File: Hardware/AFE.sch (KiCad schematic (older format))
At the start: 43 parts, among them U801 4069.HEF4069UBTT,118, U802 MCP47CXBX2

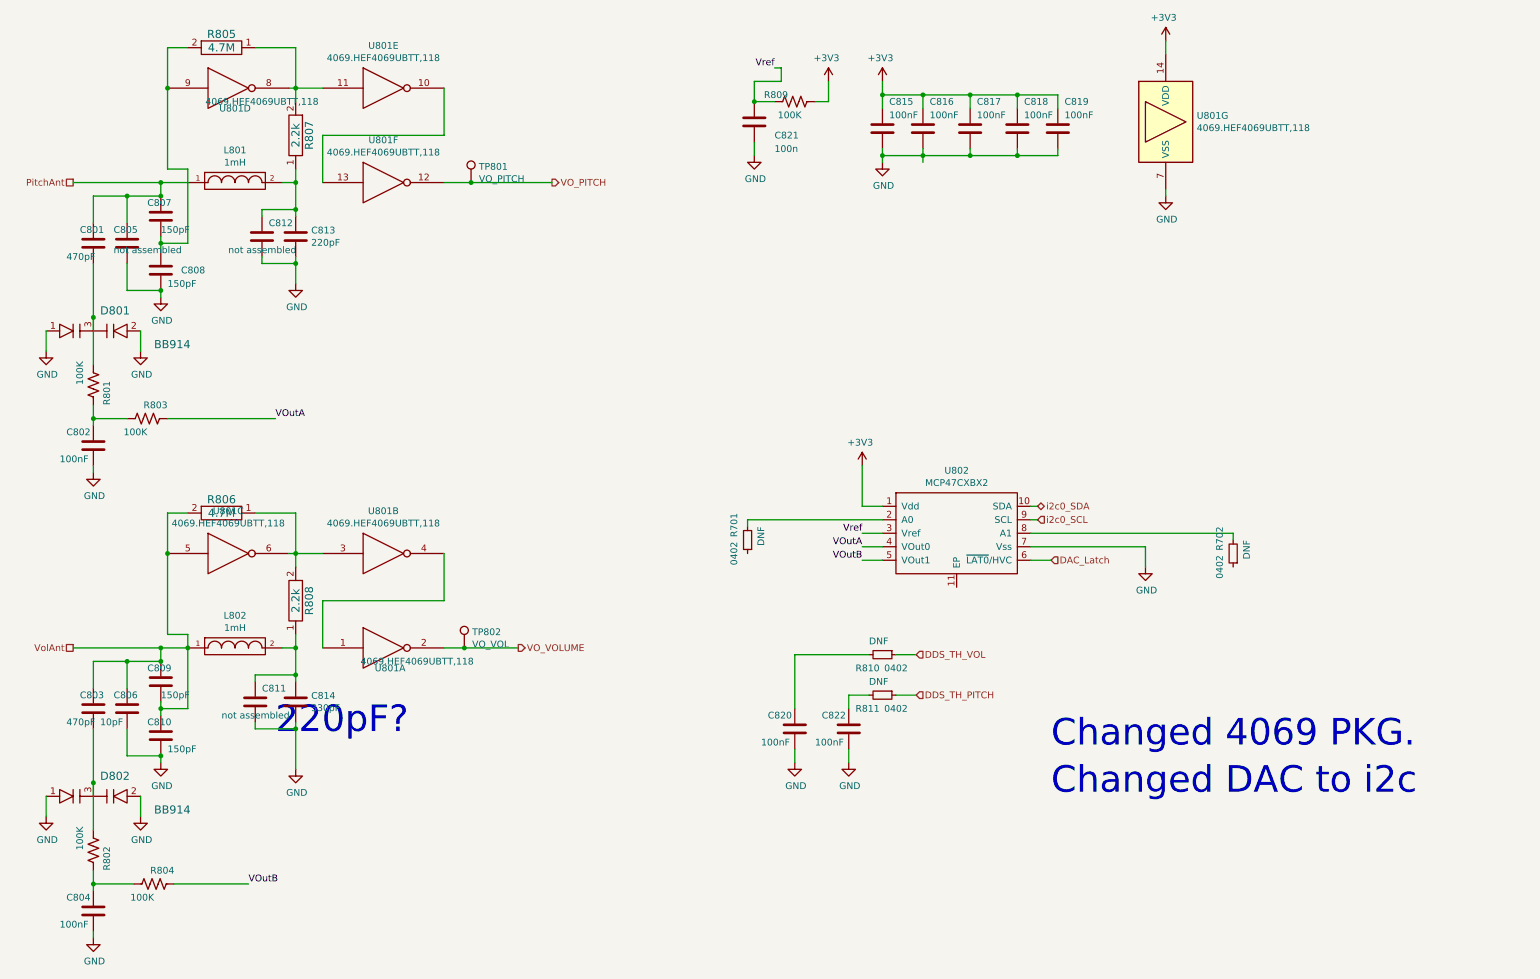
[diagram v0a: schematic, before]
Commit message: Fixing up some BoM repetition.
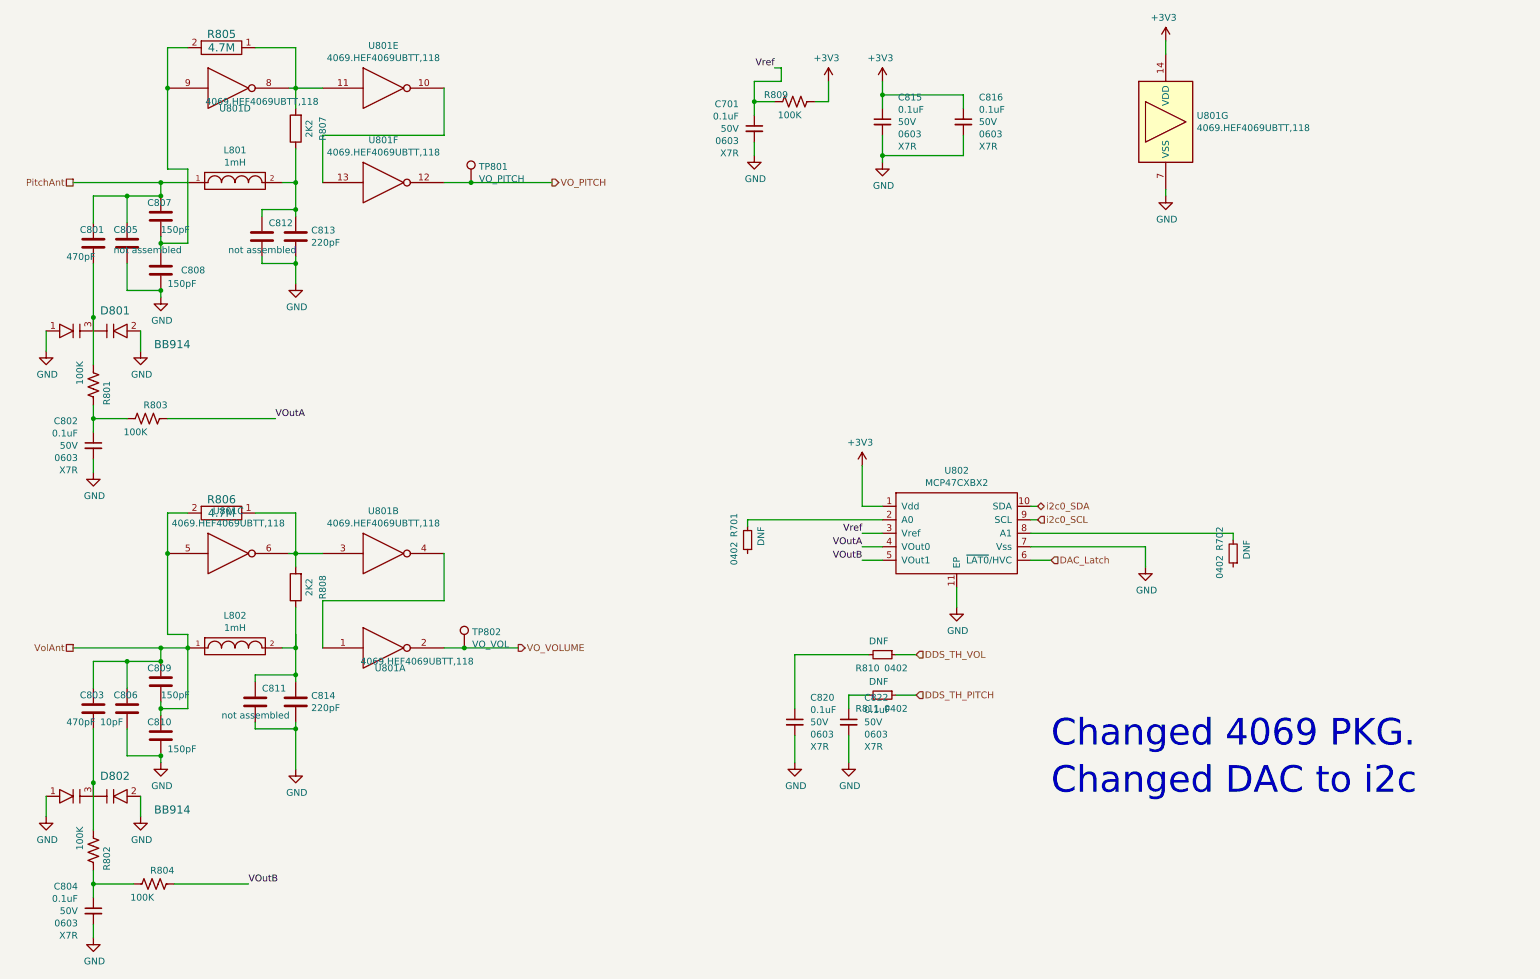
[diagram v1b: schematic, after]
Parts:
- removed C802, C804, C815, C816, C817, C818, C819, C820, C822: 100nF, Capacitor_SMD:C_0603_1608Metric_Pad1.08x0.95mm_HandSolder, symbol Device:C
- removed C821: 100n, Capacitor_SMD:C_0603_1608Metric_Pad1.08x0.95mm_HandSolder, symbol Device:C
- removed R807, R808: 2.2k, Resistor_SMD:R_0603_1608Metric_Pad0.98x0.95mm_HandSolder, symbol OpenThereminCC-rescue:RES
- added C701, C802, C804, C815, C816, C820, C822: 0.1uF, Capacitor_SMD:C_0603_1608Metric, symbol Device:C_Small
- added R807, R808: 2K2, Resistor_SMD:R_0603_1608Metric, symbol Device:R
- C813: footprint Capacitor_SMD:C_0603_1608Metric_Pad1.08x0.95mm_HandSolder -> Capacitor_SMD:C_0603_1608Metric
- C814: value 330pF -> 220pF
- R805, R806: footprint Resistor_SMD:R_0603_1608Metric_Pad0.98x0.95mm_HandSolder -> Resistor_SMD:R_0603_1608Metric
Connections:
- net +3V3: now also C815.1, C816.1
- net GND: now also U802.11 (EP), C701.2, C802.2, C804.2, C815.2, C816.2, C820.2, C822.2
- net Vref: now also C701.1
- net at R806.1, U801.3, U801.6: now also R808.2
- net at C812.1, C813.1, L801.2: now also R807.1
- net at R805.1, U801.11, U801.8: now also R807.2
- net at R801.2, R803.1: now also C802.1
- net at C811.1, C814.1, L802.2: now also R808.1
- net at R802.2, R804.1: now also C804.1
- net at R811.2: now also C822.1
- net at R810.2: now also C820.1
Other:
- note removed: "220pF?\n"

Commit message: Placements mostly done.
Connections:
- net at C804.1, R802.2: no longer R804.1
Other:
- moved on the sheet: R804
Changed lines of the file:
@@
 L Device:R_US R?
 U 1 1 6165DF0B
-P 1500 7000
+P 1550 7000
 AR Path="/611E335F/6165DF0B" Ref="R?"  Part="1"
 AR Path="/612429E8/6165DF0B" Ref="R804"  Part="1"
-F 0 "R804" V 1600 6850 50  0000 L CNN
-F 1 "100K" V 1400 7000 50  0000 L CNN
-F 2 "Resistor_SMD:R_0603_1608Metric" V 1430 7000 50  0001 C CNN
-F 3 "~" H 1500 7000 50  0001 C CNN
-F 4 "0603" H 1500 7000 50  0001 C CNN "Pkg"
-F 5 "ESR03EZPJ104" H 1500 7000 50  0001 C CNN "MPN"
-F 6 "RHM100KDCT-ND" H 1500 7000 50  0001 C CNN "DPN"
-	1    1500 7000
+F 0 "R804" V 1650 6850 50  0000 L CNN
+F 1 "100K" V 1450 7000 50  0000 L CNN
+F 2 "Resistor_SMD:R_0603_1608Metric" V 1480 7000 50  0001 C CNN
+F 3 "~" H 1550 7000 50  0001 C CNN
+F 4 "0603" H 1550 7000 50  0001 C CNN "Pkg"
+F 5 "ESR03EZPJ104" H 1550 7000 50  0001 C CNN "MPN"
+F 6 "RHM100KDCT-ND" H 1550 7000 50  0001 C CNN "DPN"
+	1    1550 7000
 	0    -1   -1   0
 $EndComp
 Wire Wire Line
-	1650 7000 2200 7000
+	1700 7000 2250 7000
 Wire Wire Line
 	1050 7000 1350 7000

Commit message: Most placements, testpoints and spare points added. Looking good.
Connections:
- net VO_PITCH: now also C822.1, R811.2
- net VO_VOLUME: now also C820.1, R810.2
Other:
- note removed: "Changed 4069 PKG."
- note removed: "Changed DAC to i2c"
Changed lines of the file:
@@
 Wire Wire Line
 	2550 2400 2550 2550
-Text Notes 8150 6350 0    197  ~ 0
-Changed DAC to i2c
 $Comp
 L OHMC2022:MCP47CXBX2 U802
@@
 Text HLabel 900  5250 0    50   UnSpc ~ 0
 VolAnt
-Text HLabel 4450 1800 2    50   Output ~ 0
+Text HLabel 4950 1800 2    50   Output ~ 0
 VO_PITCH
-Text HLabel 4200 5250 2    50   Output ~ 0
+Text HLabel 4700 5250 2    50   Output ~ 0
 VO_VOLUME
 Text HLabel 8050 4200 2    50   BiDi ~ 0
@@
 Wire Wire Line
 	1750 5250 1750 5150
-Text Notes 8150 6000 0    197  ~ 0
-Changed 4069 PKG.
 Wire Wire Line
 	900  1800 1550 1800
@@
 Connection ~ 3800 5250
 Wire Wire Line
-	3800 5250 4200 5250
+	3800 5250 4700 5250
 Wire Wire Line
 	3650 1800 3850 1800
 Connection ~ 3850 1800
 Wire Wire Line
-	3850 1800 4450 1800
+	3850 1800 4950 1800
 Wire Wire Line
 	6750 4500 6900 4500
@@
 Wire Wire Line
 	2550 4950 2550 5250
+Text Label 4200 5250 0    50   ~ 0
+VO_VOLUME
+Text Label 6250 5300 0    50   ~ 0
+VO_VOLUME
+Text Label 4450 1800 0    50   ~ 0
+VO_PITCH
+Text Label 6700 5600 2    50   ~ 0
+VO_PITCH
 $EndSCHEMATC

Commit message: Spare points on r=26.5mm @ x1.27mm linear separation.
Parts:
- added JP?: DAC_A0, OHMC2022:SolderJumper-3_P1.3mm_Open_RoundedPad1.0x1.5mm, symbol Jumper:SolderJumper_3_Open
- added JP?: DAC_A1, OHMC2022:SolderJumper-3_P1.3mm_Open_RoundedPad1.0x1.5mm, symbol Jumper:SolderJumper_3_Open
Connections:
- wire segments 138 -> 141
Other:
- moved on the sheet: R701, R702
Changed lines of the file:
@@
 L Device:R_Small R?
 U 1 1 614FE799
-P 5900 4450
+P 6400 4300
 AR Path="/611E335F/614FE799" Ref="R?"  Part="1"
 AR Path="/614FE799" Ref="R?"  Part="1"
 AR Path="/611E3335/614FE799" Ref="R?"  Part="1"
 AR Path="/612429E8/614FE799" Ref="R701"  Part="1"
-F 0 "R701" V 6000 4250 50  0000 L CNN
-F 1 "DNF" V 5800 4350 50  0000 L CNN
-F 2 "Resistor_SMD:R_0402_1005Metric" V 5830 4450 50  0001 C CNN
-F 3 "~" H 5900 4450 50  0001 C CNN
-F 4 "0402" V 6000 4550 50  0000 C CNN "Pkg"
-F 5 "" H 5900 4450 50  0001 C CNN "MPN"
-F 6 "" H 5900 4450 50  0001 C CNN "DPN"
-	1    5900 4450
-	-1   0    0    1
+F 0 "R701" V 6500 4100 50  0000 L CNN
+F 1 "DNF" V 6300 4200 50  0000 L CNN
+F 2 "Resistor_SMD:R_0402_1005Metric" V 6330 4300 50  0001 C CNN
+F 3 "~" H 6400 4300 50  0001 C CNN
+F 4 "0402" V 6500 4400 50  0000 C CNN "Pkg"
+F 5 "" H 6400 4300 50  0001 C CNN "MPN"
+F 6 "" H 6400 4300 50  0001 C CNN "DPN"
+	1    6400 4300
+	0    -1   -1   0
 $EndComp
 $Comp
 L Device:R_Small R?
 U 1 1 614FEE62
-P 9500 4550
+P 9000 4400
 AR Path="/611E335F/614FEE62" Ref="R?"  Part="1"
 AR Path="/614FEE62" Ref="R?"  Part="1"
 AR Path="/611E3335/614FEE62" Ref="R?"  Part="1"
 AR Path="/612429E8/614FEE62" Ref="R702"  Part="1"
-F 0 "R702" V 9600 4350 50  0000 L CNN
-F 1 "DNF" V 9400 4450 50  0000 L CNN
-F 2 "Resistor_SMD:R_0402_1005Metric" V 9430 4550 50  0001 C CNN
-F 3 "~" H 9500 4550 50  0001 C CNN
-F 4 "0402" V 9600 4650 50  0000 C CNN "Pkg"
-F 5 "" H 9500 4550 50  0001 C CNN "MPN"
-F 6 "" H 9500 4550 50  0001 C CNN "DPN"
-	1    9500 4550
-	-1   0    0    1
-$EndComp
-Wire Wire Line
-	8000 4400 9500 4400
-Wire Wire Line
-	9500 4400 9500 4450
-Wire Wire Line
-	5900 4300 5900 4350
-Wire Wire Line
-	5900 4300 6900 4300
+F 0 "R702" V 9100 4200 50  0000 L CNN
+F 1 "DNF" V 8900 4300 50  0000 L CNN
+F 2 "Resistor_SMD:R_0402_1005Metric" V 8930 4400 50  0001 C CNN
+F 3 "~" H 9000 4400 50  0001 C CNN
+F 4 "0402" V 9100 4500 50  0000 C CNN "Pkg"
+F 5 "" H 9000 4400 50  0001 C CNN "MPN"
+F 6 "" H 9000 4400 50  0001 C CNN "DPN"
+	1    9000 4400
+	0    -1   -1   0
+$EndComp
+Wire Wire Line
+	8000 4400 8900 4400
+Wire Wire Line
+	6500 4300 6900 4300
 $Comp
 L power:GND #PWR0141
@@
 Text Label 6700 5600 2    50   ~ 0
 VO_PITCH
+$Comp
+L Jumper:SolderJumper_3_Open JP?
+U 1 1 61714625
+P 6150 4300
+AR Path="/61714625" Ref="JP?"  Part="1"
+AR Path="/612429E8/61714625" Ref="JP?"  Part="1"
+F 0 "JP?" H 6150 4505 50  0000 C CNN
+F 1 "DAC_A0" H 6150 4414 50  0000 C CNN
+F 2 "OHMC2022:SolderJumper-3_P1.3mm_Open_RoundedPad1.0x1.5mm" H 6150 4300 50  0001 C CNN
+F 3 "~" H 6150 4300 50  0001 C CNN
+	1    6150 4300
+	0    -1   -1   0
+$EndComp
+$Comp
+L Jumper:SolderJumper_3_Open JP?
+U 1 1 61720361
+P 9250 4400
+AR Path="/61720361" Ref="JP?"  Part="1"
+AR Path="/612429E8/61720361" Ref="JP?"  Part="1"
+F 0 "JP?" H 9250 4605 50  0000 C CNN
+F 1 "DAC_A1" H 9250 4514 50  0000 C CNN
+F 2 "OHMC2022:SolderJumper-3_P1.3mm_Open_RoundedPad1.0x1.5mm" H 9250 4400 50  0001 C CNN
+F 3 "~" H 9250 4400 50  0001 C CNN
+	1    9250 4400
+	0    1    -1   0
+$EndComp
+$Comp
+L power:+3V3 #PWR?
+U 1 1 6172140B
+P 6150 3900
+AR Path="/611E3335/6172140B" Ref="#PWR?"  Part="1"
+AR Path="/6172140B" Ref="#PWR?"  Part="1"
+AR Path="/612429E8/6172140B" Ref="#PWR?"  Part="1"
+F 0 "#PWR?" H 6150 3750 50  0001 C CNN
+F 1 "+3V3" H 6165 4073 50  0000 C CNN
+F 2 "" H 6150 3900 50  0001 C CNN
+F 3 "" H 6150 3900 50  0001 C CNN
+	1    6150 3900
+	-1   0    0    -1
+$EndComp
+Wire Wire Line
+	6150 3900 6150 4100
+$Comp
+L power:GND #PWR?
+U 1 1 617275D5
+P 6150 4650
+F 0 "#PWR?" H 6150 4400 50  0001 C CNN
+F 1 "GND" H 6158 4477 50  0000 C CNN
+F 2 "" H 6150 4650 50  0000 C CNN
+F 3 "" H 6150 4650 50  0000 C CNN
+	1    6150 4650
+	1    0    0    -1
+$EndComp
+Wire Wire Line
+	6150 4500 6150 4650
+$Comp
+L power:+3V3 #PWR?
+U 1 1 6172EEF6
+P 9250 4000
+AR Path="/611E3335/6172EEF6" Ref="#PWR?"  Part="1"
+AR Path="/6172EEF6" Ref="#PWR?"  Part="1"
+AR Path="/612429E8/6172EEF6" Ref="#PWR?"  Part="1"
+F 0 "#PWR?" H 9250 3850 50  0001 C CNN
+F 1 "+3V3" H 9265 4173 50  0000 C CNN
+F 2 "" H 9250 4000 50  0001 C CNN
+F 3 "" H 9250 4000 50  0001 C CNN
+	1    9250 4000
+	-1   0    0    -1
+$EndComp
+Wire Wire Line
+	9250 4000 9250 4200
+$Comp
+L power:GND #PWR?
+U 1 1 6173729C
+P 9250 4700
+F 0 "#PWR?" H 9250 4450 50  0001 C CNN
+F 1 "GND" H 9258 4527 50  0000 C CNN
+F 2 "" H 9250 4700 50  0000 C CNN
+F 3 "" H 9250 4700 50  0000 C CNN
+	1    9250 4700
+	1    0    0    -1
+$EndComp
+Wire Wire Line
+	9250 4550 9250 4600
+Connection ~ 9250 4600
+Wire Wire Line
+	9250 4600 9250 4700
 $EndSCHEMATC

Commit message: Doing finer aspirational placements.
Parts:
- gave numbers to parts that had none: 2
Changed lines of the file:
@@
 P 6150 4300
 AR Path="/61714625" Ref="JP?"  Part="1"
-AR Path="/612429E8/61714625" Ref="JP?"  Part="1"
-F 0 "JP?" H 6150 4505 50  0000 C CNN
+AR Path="/612429E8/61714625" Ref="JP401"  Part="1"
+F 0 "JP401" H 6150 4505 50  0000 C CNN
 F 1 "DAC_A0" H 6150 4414 50  0000 C CNN
 F 2 "OHMC2022:SolderJumper-3_P1.3mm_Open_RoundedPad1.0x1.5mm" H 6150 4300 50  0001 C CNN
@@
 P 9250 4400
 AR Path="/61720361" Ref="JP?"  Part="1"
-AR Path="/612429E8/61720361" Ref="JP?"  Part="1"
-F 0 "JP?" H 9250 4605 50  0000 C CNN
+AR Path="/612429E8/61720361" Ref="JP402"  Part="1"
+F 0 "JP402" H 9250 4605 50  0000 C CNN
 F 1 "DAC_A1" H 9250 4514 50  0000 C CNN
 F 2 "OHMC2022:SolderJumper-3_P1.3mm_Open_RoundedPad1.0x1.5mm" H 9250 4400 50  0001 C CNN
@@
 AR Path="/611E3335/6172140B" Ref="#PWR?"  Part="1"
 AR Path="/6172140B" Ref="#PWR?"  Part="1"
-AR Path="/612429E8/6172140B" Ref="#PWR?"  Part="1"
-F 0 "#PWR?" H 6150 3750 50  0001 C CNN
+AR Path="/612429E8/6172140B" Ref="#PWR0197"  Part="1"
+F 0 "#PWR0197" H 6150 3750 50  0001 C CNN
 F 1 "+3V3" H 6165 4073 50  0000 C CNN
 F 2 "" H 6150 3900 50  0001 C CNN
@@
 	6150 3900 6150 4100
 $Comp
-L power:GND #PWR?
+L power:GND #PWR0198
 U 1 1 617275D5
 P 6150 4650
-F 0 "#PWR?" H 6150 4400 50  0001 C CNN
+F 0 "#PWR0198" H 6150 4400 50  0001 C CNN
 F 1 "GND" H 6158 4477 50  0000 C CNN
 F 2 "" H 6150 4650 50  0000 C CNN
@@
 AR Path="/611E3335/6172EEF6" Ref="#PWR?"  Part="1"
 AR Path="/6172EEF6" Ref="#PWR?"  Part="1"
-AR Path="/612429E8/6172EEF6" Ref="#PWR?"  Part="1"
-F 0 "#PWR?" H 9250 3850 50  0001 C CNN
+AR Path="/612429E8/6172EEF6" Ref="#PWR0199"  Part="1"
+F 0 "#PWR0199" H 9250 3850 50  0001 C CNN
 F 1 "+3V3" H 9265 4173 50  0000 C CNN
 F 2 "" H 9250 4000 50  0001 C CNN
@@
 	9250 4000 9250 4200
 $Comp
-L power:GND #PWR?
+L power:GND #PWR0200
 U 1 1 6173729C
 P 9250 4700
-F 0 "#PWR?" H 9250 4450 50  0001 C CNN
+F 0 "#PWR0200" H 9250 4450 50  0001 C CNN
 F 1 "GND" H 9258 4527 50  0000 C CNN
 F 2 "" H 9250 4700 50  0000 C CNN
